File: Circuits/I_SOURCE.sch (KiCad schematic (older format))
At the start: 27 parts, among them P1 +8, P2 -8, P3 GND, P4 OUTPUT, Q1 TIP126, U1 CA3140, U2 LM393

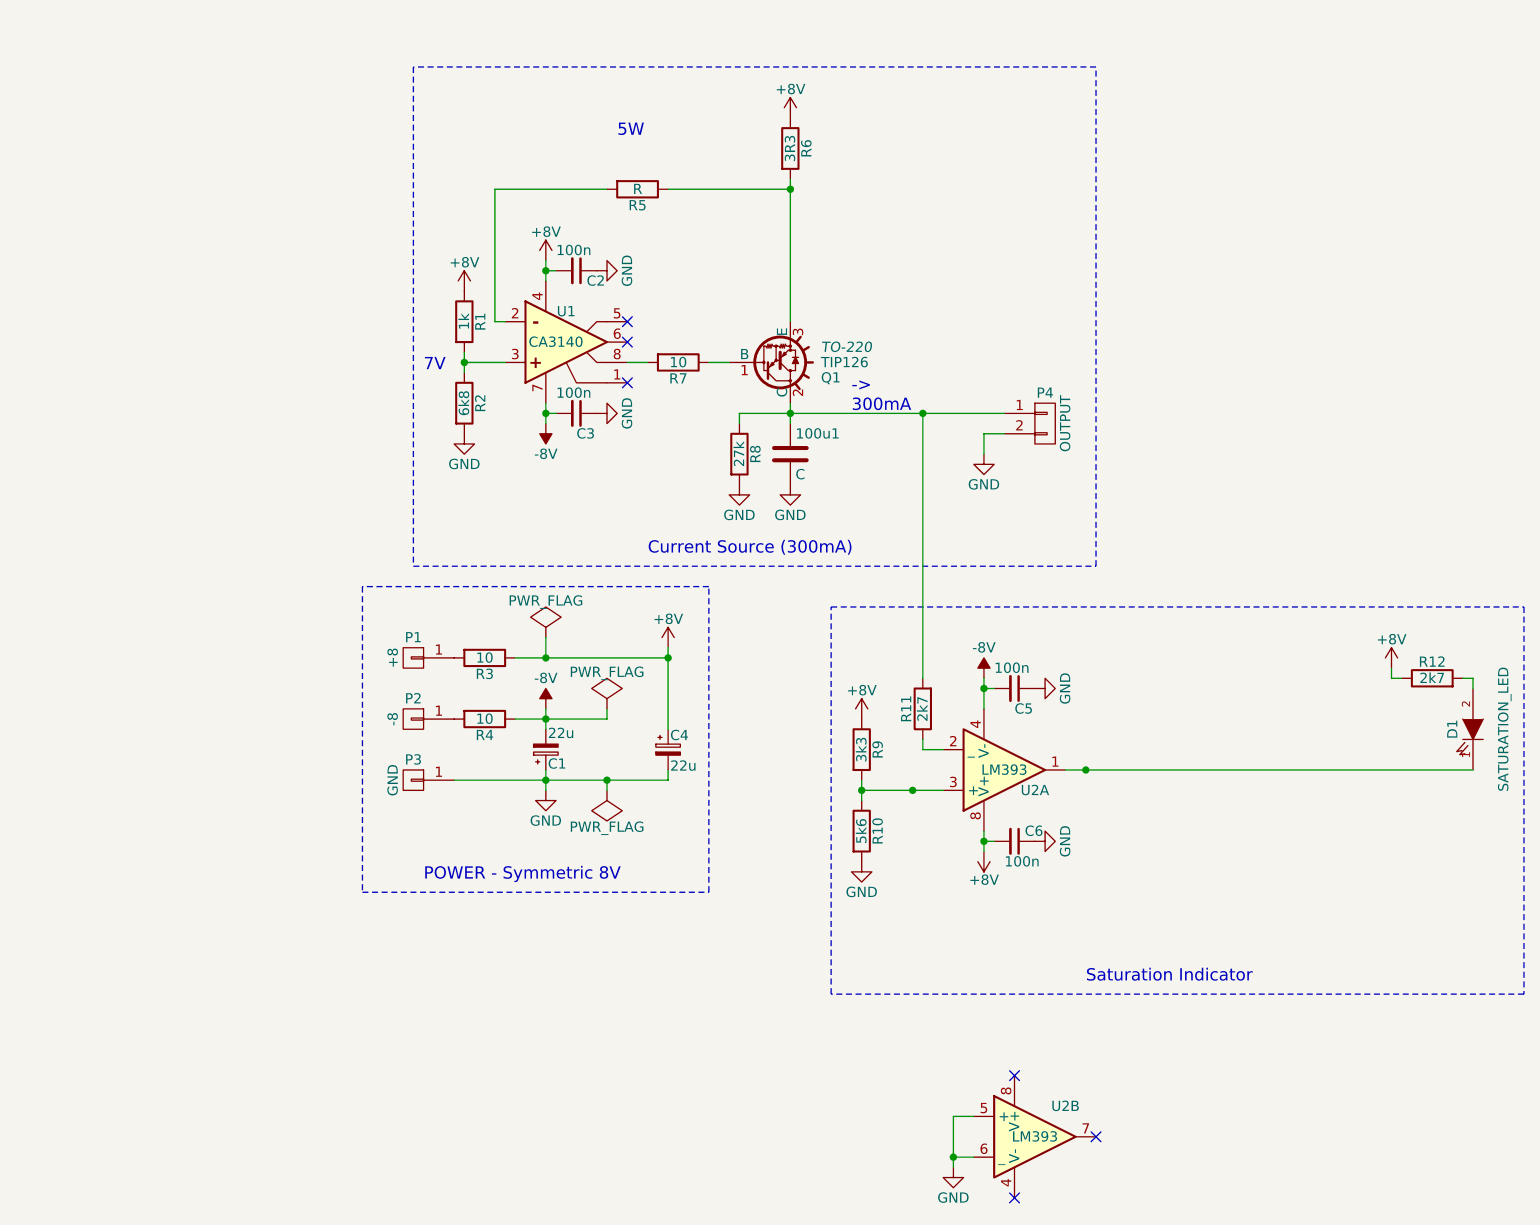
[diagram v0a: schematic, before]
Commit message: ADD: Schematic Documentation
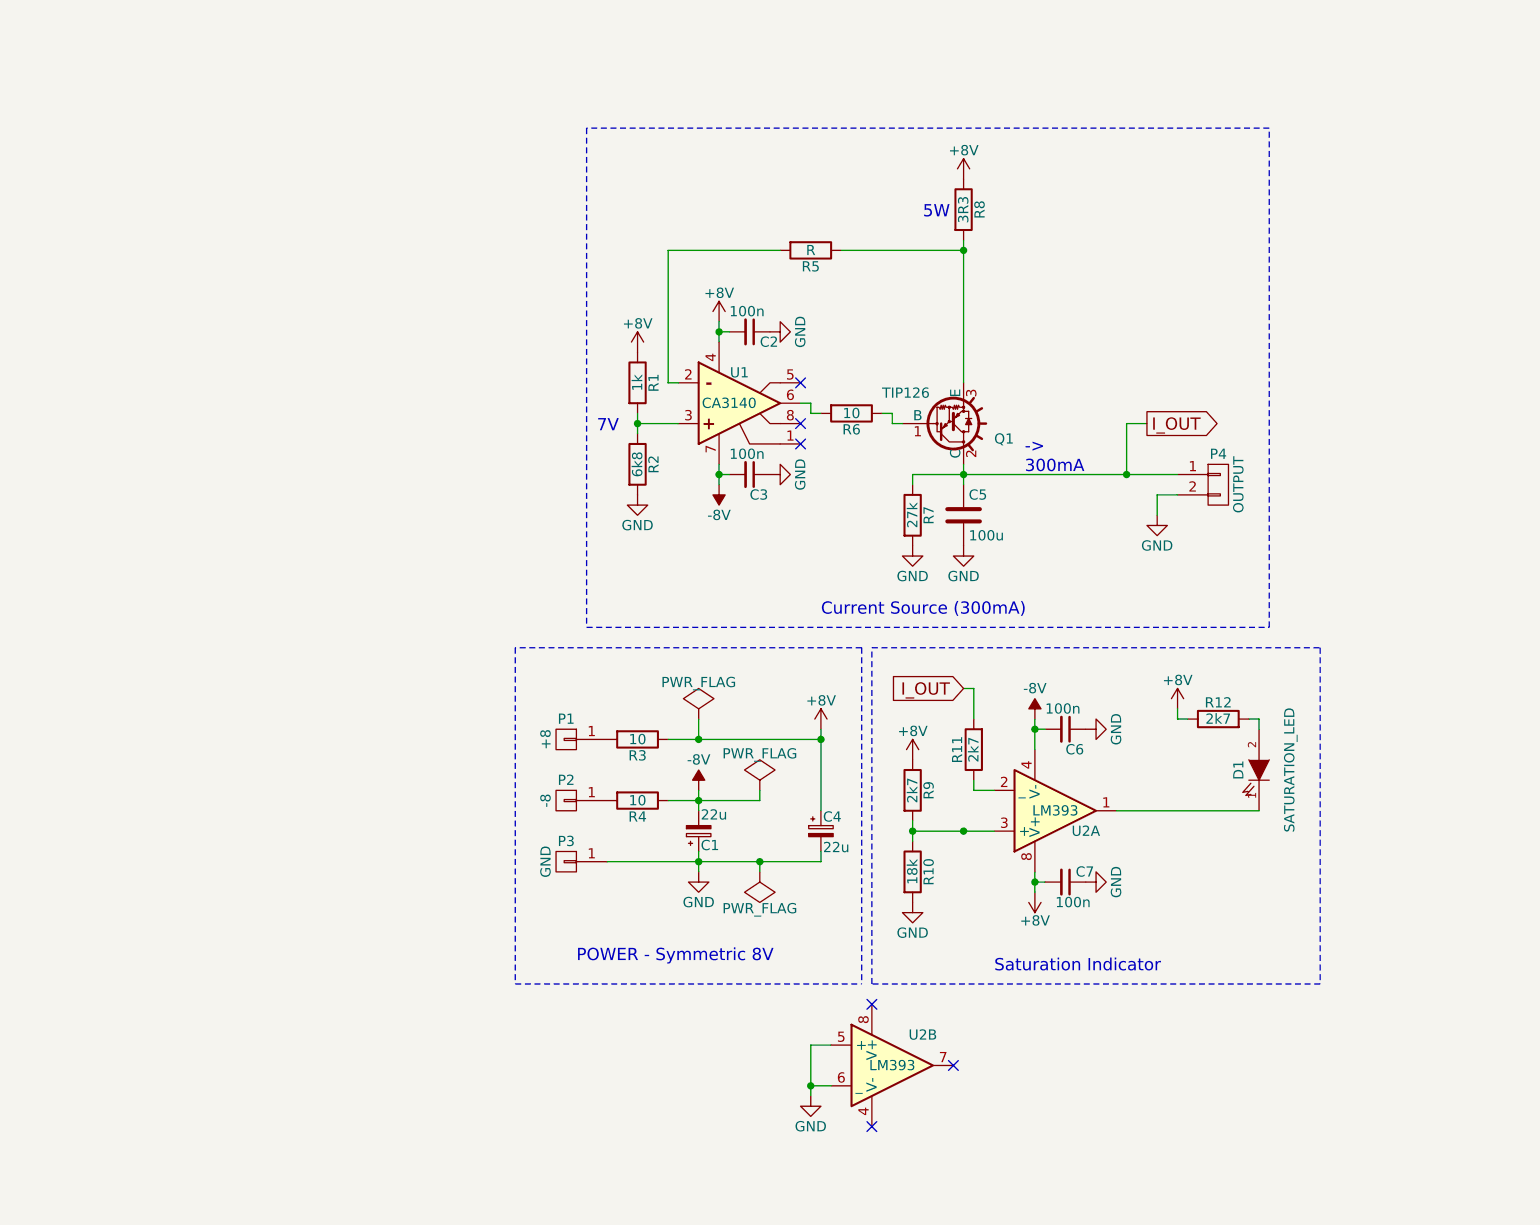
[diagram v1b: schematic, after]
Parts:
- C5: renamed from 100u1; value C -> 100u
- R10: value 5k6 -> 18k
- R9: value 3k3 -> 2k7
- renumbered C5 to C6, C6 to C7, R7 to R6, R8 to R7, R6 to R8
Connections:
- net at U1.6 (OUTPUT): now also R6.2
- net at U1.8 (COMP): no longer R6.2
- net I_OUT: now reaches C5.1, P4.1 (P1), Q1.2 (C), R11.2, R7.1
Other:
- moved on the sheet: C1, C2, C3, C4, C5, C6, C7, D1, P1, P2, P3, P4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

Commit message: Added full schematics and power supply
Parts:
- added P5: I_SELECT, symbol CONN_01X03
- added R13: 2R, symbol R
- Q1: value TIP126 -> TIP127
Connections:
- net +8V: now also R13.1
- net at Q1.3 (E), R5.1: now also P5.2 (P2); no longer R8.2
- new net: P5.3 (P3), R8.2
- new net: P5.1 (P1), R13.2
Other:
- note added: "->\n300/500mA\n"
- note added: "300mA\n"
- note added: "500mA\n"
- note added: "Common"
- note added: "Current Source (300/500mA)"
- note removed: "->\n300mA\n"
- note removed: "Current Source (300mA)"
- moved on the sheet: C1, C2, C3, C4, C5, C6, C7, D1, P1, P2, P3, P4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
